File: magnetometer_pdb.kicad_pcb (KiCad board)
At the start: 2 copper layers, 98 x 87.5 mm, 68 parts, among them J1 Screw_Terminal_01x02, J10 Screw_Terminal_01x02, J11 Screw_Terminal_01x02, J12 Screw_Terminal_01x02, J13 Screw_Terminal_01x02, J14 Screw_Terminal_01x02, J15 Conn_01x02_Pin, J2 Screw_Terminal_01x02, J3 Screw_Terminal_01x02, J4 Screw_Terminal_01x02, J5 Screw_Terminal_01x02, J6 Conn_01x02_Pin, J7 Conn_01x02_Pin, J8 Conn_01x02_Pin, J9 Screw_Terminal_01x02, U1 TPS56528DDA, U2 L78L09_SO8

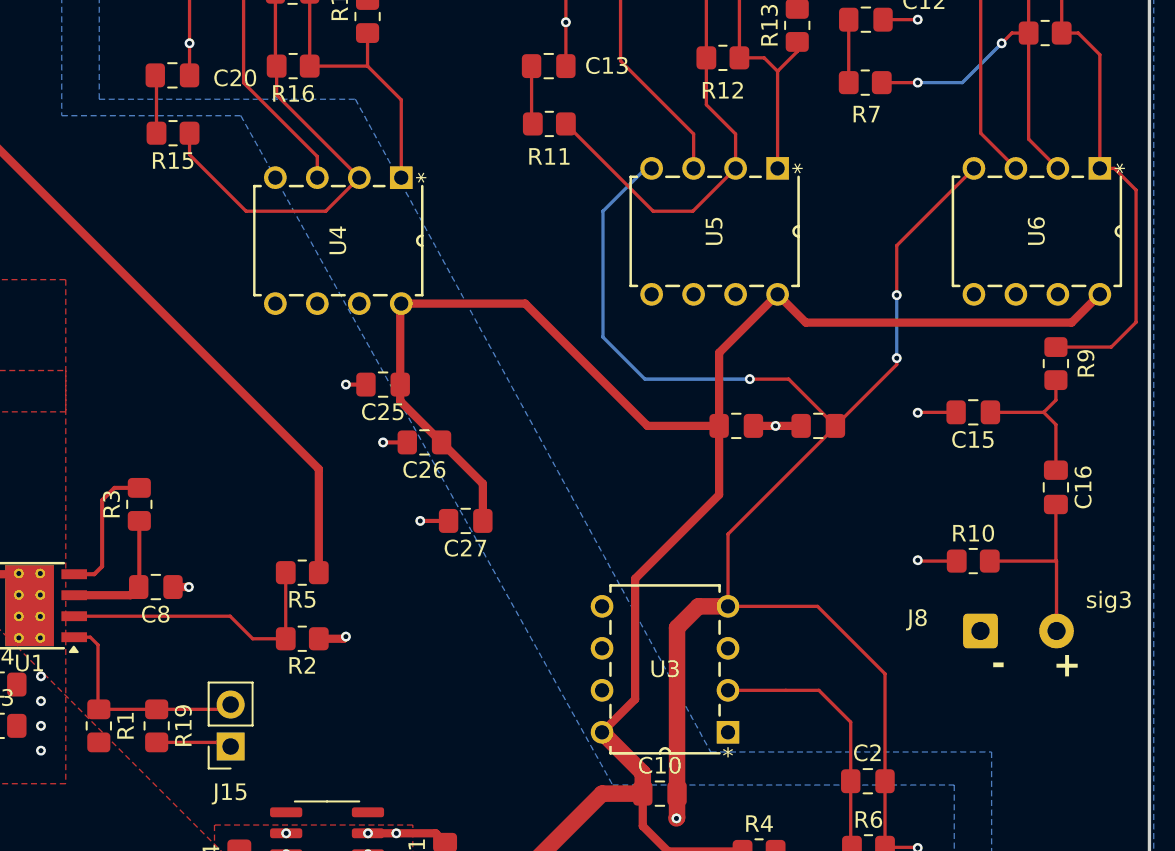
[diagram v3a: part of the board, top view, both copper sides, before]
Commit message: Adjusted caps
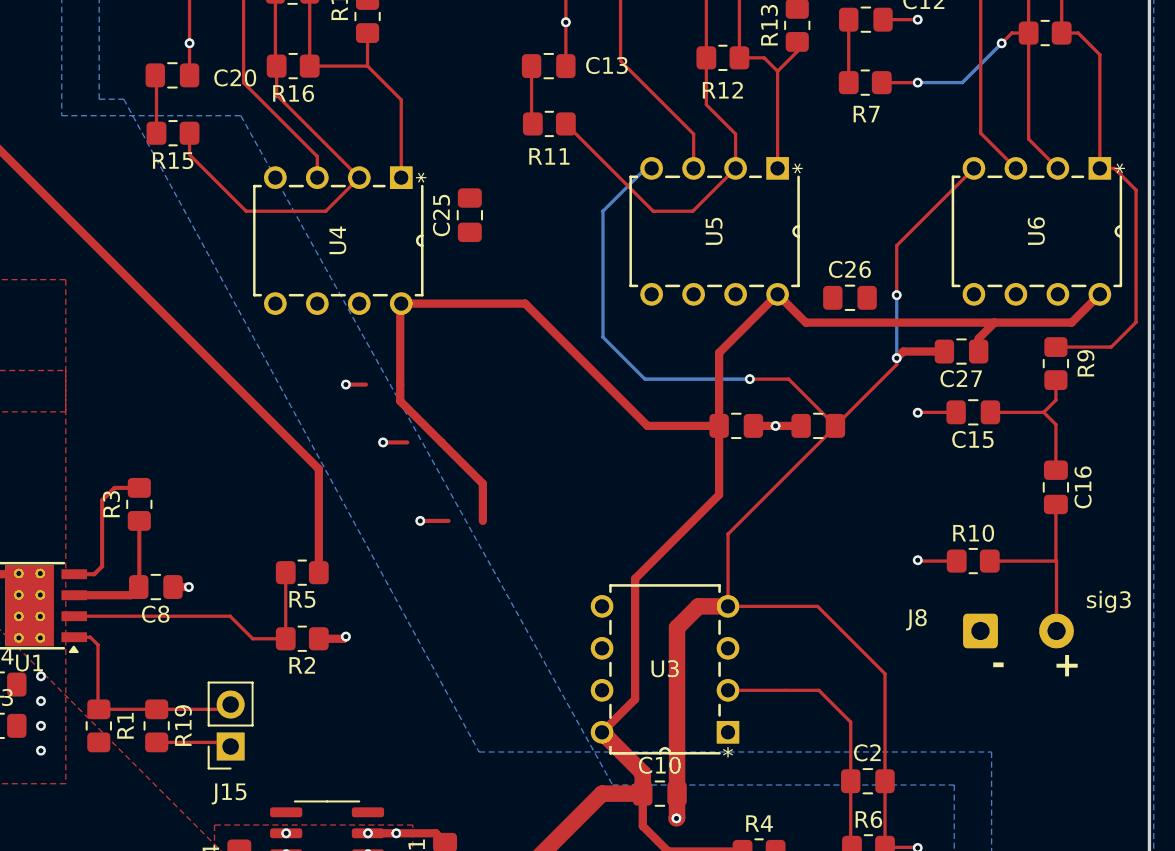
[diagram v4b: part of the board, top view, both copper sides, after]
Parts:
- moved C27 31.7 mm to (104.2, 56.8)
- moved C26 27.2 mm to (97.5, 53.5), turned to 0 degrees
- moved C25 11.5 mm to (74.5, 48.5), turned to 90 degrees
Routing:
- net Bat_GND: track 119.7 -> 122.8 mm
- net 9V_out: track 121.5 -> 123.6 mm
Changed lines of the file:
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@@
 	(footprint "Capacitor_SMD:C_0805_2012Metric_Pad1.18x1.45mm_HandSolder"
 		(layer "F.Cu")
-		(at 69.25 58.75 180)
+		(at 74.5 48.5 90)
 		(descr "Capacitor SMD 0805 (2012 Metric), square (rectangular) end terminal, IPC-7351 nominal with elongated pad for handsoldering. (Body size source: IPC-SM-782 page 76, https://www.pcb-3d.com/wordpress/wp-content/uploads/ipc-sm-782a_amendment_1_and_2.pdf, https://docs.google.com/spreadsheets/d/1BsfQQcO9C6DZCsRaXUlFlo91Tg2WpOkGARC1WS5S8t0/edit?usp=sharing), generated with kicad-footprint-generator")
 		(tags "capacitor handsolder")
 		(property "Reference" "C25"
-			(at 0 -1.68 0)
+			(at 0 -1.68 90)
 			(layer "F.SilkS")
 			(effects
@@
 		)
 		(property "Value" "2.2u"
-			(at 0 1.68 0)
+			(at 0 1.68 90)
 			(layer "F.Fab")
 			(effects
@@
 		)
 		(property "Datasheet" ""
-			(at 0 0 0)
+			(at 0 0 90)
 			(layer "F.Fab")
 			(hide yes)
@@
 		)
 		(property "Description" "Unpolarized capacitor, small symbol"
-			(at 0 0 0)
+			(at 0 0 90)
 			(layer "F.Fab")
 			(hide yes)
@@
 		(attr smd)
 		(fp_line
-			(start -0.261252 0.735)
-			(end 0.261252 0.735)
+			(start -0.261252 -0.735)
+			(end 0.261252 -0.735)
 			(stroke
 				(width 0.12)
@@
 		)
 		(fp_line
-			(start -0.261252 -0.735)
-			(end 0.261252 -0.735)
+			(start -0.261252 0.735)
+			(end 0.261252 0.735)
 			(stroke
 				(width 0.12)
@@
 		)
 		(fp_line
-			(start 1.88 0.98)
-			(end -1.88 0.98)
+			(start 1.88 -0.98)
+			(end 1.88 0.98)
 			(stroke
 				(width 0.05)
@@
 		)
 		(fp_line
-			(start 1.88 -0.98)
-			(end 1.88 0.98)
+			(start -1.88 -0.98)
+			(end 1.88 -0.98)
 			(stroke
 				(width 0.05)
@@
 		)
 		(fp_line
-			(start -1.88 0.98)
-			(end -1.88 -0.98)
+			(start 1.88 0.98)
+			(end -1.88 0.98)
 			(stroke
 				(width 0.05)
@@
 		)
 		(fp_line
-			(start -1.88 -0.98)
-			(end 1.88 -0.98)
+			(start -1.88 0.98)
+			(end -1.88 -0.98)
 			(stroke
 				(width 0.05)
@@
 		)
 		(fp_line
-			(start 1 0.625)
-			(end -1 0.625)
+			(start 1 -0.625)
+			(end 1 0.625)
 			(stroke
 				(width 0.1)
@@
 		)
 		(fp_line
-			(start 1 -0.625)
-			(end 1 0.625)
+			(start -1 -0.625)
+			(end 1 -0.625)
 			(stroke
 				(width 0.1)
@@
 		)
 		(fp_line
-			(start -1 0.625)
-			(end -1 -0.625)
+			(start 1 0.625)
+			(end -1 0.625)
 			(stroke
 				(width 0.1)
@@
 		)
 		(fp_line
-			(start -1 -0.625)
-			(end 1 -0.625)
+			(start -1 0.625)
+			(end -1 -0.625)
 			(stroke
 				(width 0.1)
@@
 		)
 		(fp_text user "${REFERENCE}"
-			(at 0 0 0)
+			(at 0 0 90)
 			(layer "F.Fab")
 			(effects
@@
 		)
 		(pad "1" smd roundrect
-			(at -1.0375 0 180)
+			(at -1.0375 0 90)
 			(size 1.175 1.45)
 			(layers "F.Cu" "F.Mask" "F.Paste")
@@
 		)
 		(pad "2" smd roundrect
-			(at 1.0375 0 180)
+			(at 1.0375 0 90)
 			(size 1.175 1.45)
 			(layers "F.Cu" "F.Mask" "F.Paste")
@@
 	(footprint "Capacitor_SMD:C_0805_2012Metric_Pad1.18x1.45mm_HandSolder"
 		(layer "F.Cu")
-		(at 71.75 62.25 180)
+		(at 97.5 53.5)
 		(descr "Capacitor SMD 0805 (2012 Metric), square (rectangular) end terminal, IPC-7351 nominal with elongated pad for handsoldering. (Body size source: IPC-SM-782 page 76, https://www.pcb-3d.com/wordpress/wp-content/uploads/ipc-sm-782a_amendment_1_and_2.pdf, https://docs.google.com/spreadsheets/d/1BsfQQcO9C6DZCsRaXUlFlo91Tg2WpOkGARC1WS5S8t0/edit?usp=sharing), generated with kicad-footprint-generator")
 		(tags "capacitor handsolder")
@@
 		(attr smd)
 		(fp_line
-			(start -0.261252 0.735)
-			(end 0.261252 0.735)
+			(start -0.261252 -0.735)
+			(end 0.261252 -0.735)
 			(stroke
 				(width 0.12)
@@
 		)
 		(fp_line
-			(start -0.261252 -0.735)
-			(end 0.261252 -0.735)
+			(start -0.261252 0.735)
+			(end 0.261252 0.735)
 			(stroke
 				(width 0.12)
@@
 		)
 		(fp_line
-			(start 1.88 0.98)
-			(end -1.88 0.98)
+			(start -1.88 -0.98)
+			(end 1.88 -0.98)
 			(stroke
 				(width 0.05)
@@
 		)
 		(fp_line
-			(start 1.88 -0.98)
-			(end 1.88 0.98)
+			(start -1.88 0.98)
+			(end -1.88 -0.98)
 			(stroke
 				(width 0.05)
@@
 		)
 		(fp_line
-			(start -1.88 0.98)
-			(end -1.88 -0.98)
+			(start 1.88 -0.98)
+			(end 1.88 0.98)
 			(stroke
 				(width 0.05)
@@
 		)
 		(fp_line
-			(start -1.88 -0.98)
-			(end 1.88 -0.98)
+			(start 1.88 0.98)
+			(end -1.88 0.98)
 			(stroke
 				(width 0.05)
@@
 		)
 		(fp_line
-			(start 1 0.625)
-			(end -1 0.625)
+			(start -1 -0.625)
+			(end 1 -0.625)
 			(stroke
 				(width 0.1)
@@
 		)
 		(fp_line
-			(start 1 -0.625)
-			(end 1 0.625)
+			(start -1 0.625)
+			(end -1 -0.625)
 			(stroke
 				(width 0.1)
@@
 		)
 		(fp_line
-			(start -1 0.625)
-			(end -1 -0.625)
+			(start 1 -0.625)
+			(end 1 0.625)
 			(stroke
 				(width 0.1)
@@
 		)
 		(fp_line
-			(start -1 -0.625)
-			(end 1 -0.625)
+			(start 1 0.625)
+			(end -1 0.625)
 			(stroke
 				(width 0.1)
@@
 		)
 		(pad "1" smd roundrect
-			(at -1.0375 0 180)
+			(at -1.0375 0)
 			(size 1.175 1.45)
 			(layers "F.Cu" "F.Mask" "F.Paste")
@@
 		)
 		(pad "2" smd roundrect
-			(at 1.0375 0 180)
+			(at 1.0375 0)
 			(size 1.175 1.45)
 			(layers "F.Cu" "F.Mask" "F.Paste")
@@
 	(footprint "Capacitor_SMD:C_0805_2012Metric_Pad1.18x1.45mm_HandSolder"
 		(layer "F.Cu")
-		(at 74.25 67 180)
+		(at 104.25 56.75 180)
 		(descr "Capacitor SMD 0805 (2012 Metric), square (rectangular) end terminal, IPC-7351 nominal with elongated pad for handsoldering. (Body size source: IPC-SM-782 page 76, https://www.pcb-3d.com/wordpress/wp-content/uploads/ipc-sm-782a_amendment_1_and_2.pdf, https://docs.google.com/spreadsheets/d/1BsfQQcO9C6DZCsRaXUlFlo91Tg2WpOkGARC1WS5S8t0/edit?usp=sharing), generated with kicad-footprint-generator")
 		(tags "capacitor handsolder")
@@
 	)
 	(segment
+		(start 100.73 56.75)
+		(end 100.33 57.15)
+		(width 0.5)
+		(layer "F.Cu")
+		(net 2)
+	)
+	(segment
 		(start 87.0375 73.4625)
 		(end 88.33 72.17)
@@
 	)
 	(segment
+		(start 103.2125 56.75)
+		(end 100.73 56.75)
+		(width 0.5)
+		(layer "F.Cu")
+		(net 2)
+	)
+	(segment
 		(start 56.5375 71)
 		(end 57.5 71)
@@
 	)
 	(segment
+		(start 105.2875 55.9625)
+		(end 106.25 55)
+		(width 0.5)
+		(layer "F.Cu")
+		(net 7)
+	)
+	(segment
 		(start 70.35 53.85)
 		(end 77.85 53.85)
@@
 	(segment
 		(start 94.83 55)
-		(end 110.91 55)
+		(end 106.25 55)
 		(width 0.5)
 		(layer "F.Cu")
@@
 	)
 	(segment
+		(start 106.25 55)
+		(end 110.91 55)
+		(width 0.5)
+		(layer "F.Cu")
+		(net 7)
+	)
+	(segment
 		(start 77.85 53.85)
 		(end 85.25 61.25)
@@
 	)
 	(segment
+		(start 105.2875 56.75)
+		(end 105.2875 55.9625)
+		(width 0.5)
+		(layer "F.Cu")
+		(net 7)
+	)
+	(segment
 		(start 84.9625 82.2525)
 		(end 82.5 79.79)
@@
 		(name "GND")
 		(hatch edge 0.5)
+		(priority 4)
 		(connect_pads
 			(clearance 0)
@@
 		(polygon
 			(pts
-				(xy 52.07 14.98) (xy 52.07 41.48) (xy 67.57 41.48) (xy 89.07 80.98) (xy 106.07 80.98) (xy 106.07 102.48)
+				(xy 52.07 14.98) (xy 52.07 41.48) (xy 53.557331 41.48) (xy 75.057331 80.98) (xy 106.07 80.98) (xy 106.07 102.48)
 				(xy 115.88 102.5175) (xy 115.88 15.0175)
 			)

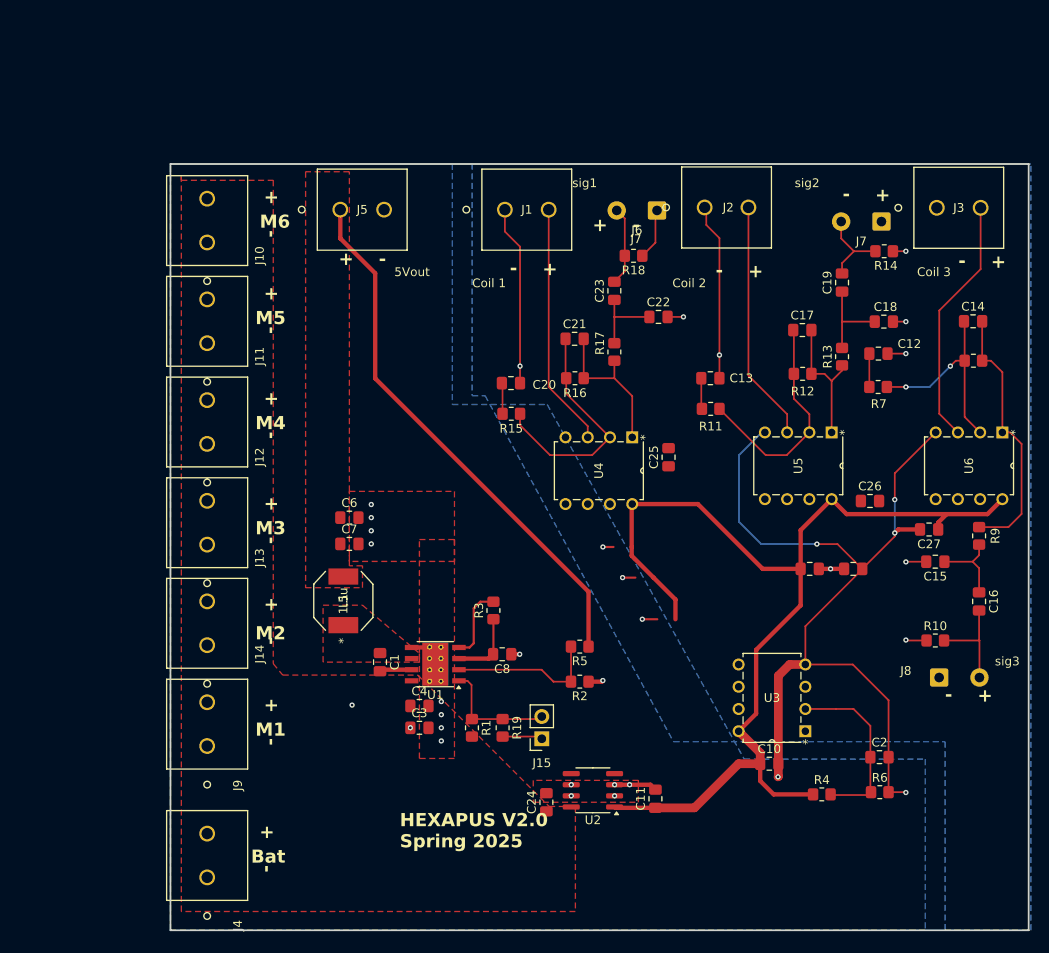
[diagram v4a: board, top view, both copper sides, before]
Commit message: Cleaned up PCB and added Fuses
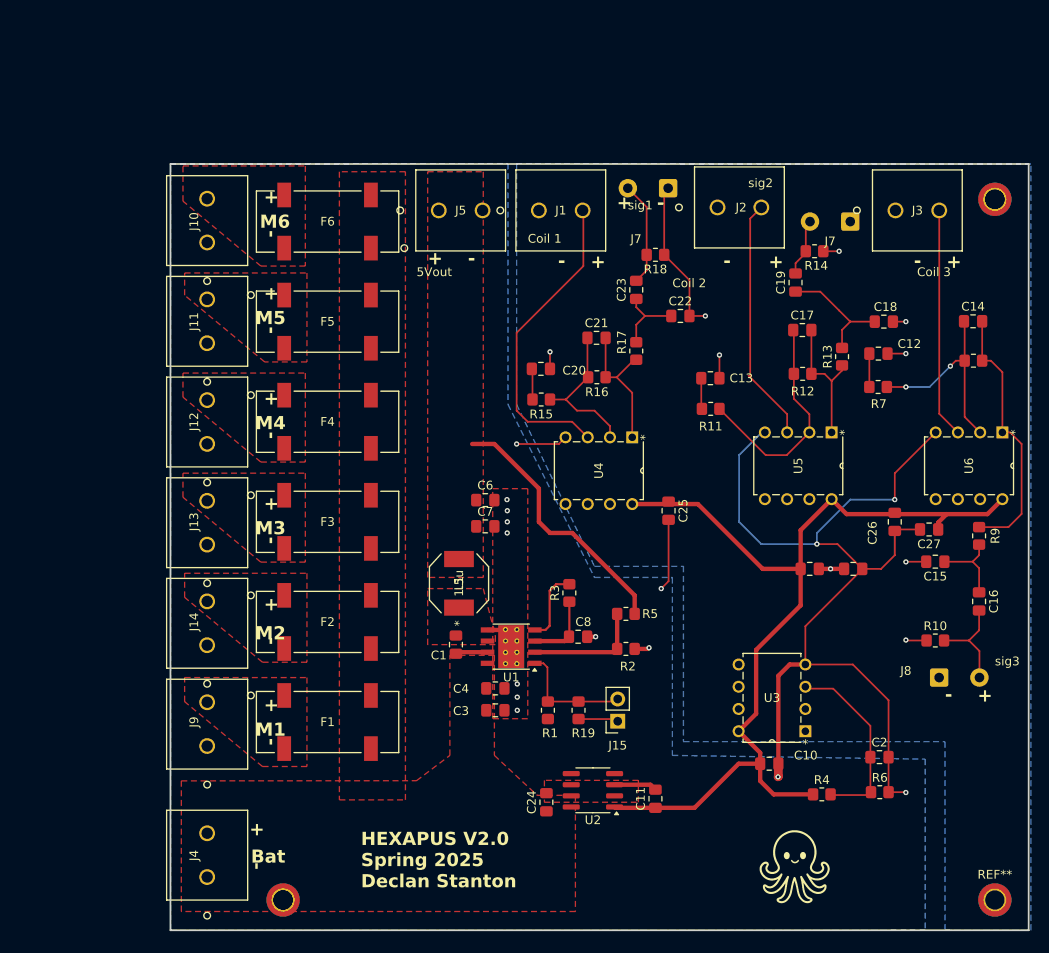
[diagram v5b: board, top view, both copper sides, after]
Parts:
- added ?: , , F.Cu at (111.8, 19.1)
- added ?: , , F.Cu at (30.5, 99.1)
- added F1: Fuse, Fuse:fuse_holder, F.Cu at (35.6, 78.7)
- added F2: Fuse, Fuse:fuse_holder, F.Cu at (35.6, 67.3)
- added F3: Fuse, Fuse:fuse_holder, F.Cu at (35.6, 55.9)
- added F4: Fuse, Fuse:fuse_holder, F.Cu at (35.6, 44.5)
- added F5: Fuse, Fuse:fuse_holder, F.Cu at (35.6, 33.0)
- added F6: Fuse, Fuse:fuse_holder, F.Cu at (35.6, 21.6)
- added G***: LOGO, Footprint:hexapus, F.Cu at (88.9, 95.2)
- added REF**: MountingHole_2.2mm_M2_DIN965_Pad_TopBottom, MountingHole:MountingHole_2.2mm_M2_DIN965_Pad_TopBottom, F.Cu at (111.8, 19.1)
- added REF**: MountingHole_2.2mm_M2_DIN965_Pad_TopBottom, MountingHole:MountingHole_2.2mm_M2_DIN965_Pad_TopBottom, F.Cu at (30.5, 99.1)
- added REF**: MountingHole_2.2mm_M2_DIN965_Pad_TopBottom, MountingHole:MountingHole_2.2mm_M2_DIN965_Pad_TopBottom, F.Cu at (111.8, 99.1)
- moved C6 15.7 mm to (53.6, 53.4)
- moved C7 15.7 mm to (53.6, 56.4)
- moved L1 13.4 mm to (50.6, 62.9)
- moved J5 11.2 mm to (48.3, 20.3)
- moved C1 8.90 mm to (50.2, 69.9)
- moved C3 8.90 mm to (54.7, 77.4)
- moved C4 8.90 mm to (54.7, 74.9)
- moved C8 8.90 mm to (64.2, 69.0)
- moved R1 8.90 mm to (60.7, 77.4)
- moved R19 8.90 mm to (64.2, 77.4)
- moved R3 8.90 mm to (63.2, 64.0)
- moved U1 8.90 mm to (56.5, 70.1)
- moved J15 8.90 mm to (68.7, 78.7)
- moved R14 7.95 mm to (91.2, 25.0)
- moved R2 6.46 mm to (69.6, 70.4)
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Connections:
- J10 pad 2: Vin -> unconnected-(J10-Pin_2-Pad2)
- J11 pad 2: Vin -> unconnected-(J11-Pin_2-Pad2)
- J12 pad 2: Vin -> unconnected-(J12-Pin_2-Pad2)
- J13 pad 2: Vin -> unconnected-(J13-Pin_2-Pad2)
- J14 pad 2: Vin -> unconnected-(J14-Pin_2-Pad2)
- J9 pad 2: Vin -> unconnected-(J9-Pin_2-Pad2)
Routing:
- net 5V_out: track 61.7 -> 31.3 mm
- net GND: track 61.0 -> 38.2 mm
- net Bat_GND: track 122.8 -> 141.8 mm, vias 24 -> 15
- net Net-(U3-+): track 4.91 -> 21.7 mm
- net (no net): track 15.7 -> 0.00 mm
- net 9V_out: track 123.6 -> 108.5 mm
- net Net-(U4--): track 27.2 -> 17.4 mm
- net Net-(J1-Pin_2): track 27.8 -> 35.4 mm
- net Net-(U1-VFB): track 17.4 -> 13.4 mm
- net Net-(C18-Pad1): track 10.3 -> 13.9 mm
- net Coil_1_sig_out: track 9.02 -> 12.0 mm
- net Coil_2_sig_out: track 9.55 -> 6.69 mm
- net Net-(J3-Pin_2): track 28.5 -> 26.2 mm
- net Net-(C21-Pad2): track 17.6 -> 16.4 mm
- net Coil_3_sig_out: track 12.5 -> 11.5 mm
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- added copper zone on F.Cu, net /M1_out
- added copper zone on F.Cu, net /M2_OUT
- added copper zone on F.Cu, net /M3_OUT
- added copper zone on F.Cu, net /M4_OUT
- added copper zone on F.Cu, net /M5_OUT
- added copper zone on F.Cu, net /M6_OUT
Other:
- board text added: "HEXAPUS V2.0 Spring 2025 Declan Stanton"
- board text removed: "HEXAPUS V2.0 Spring 2025"
